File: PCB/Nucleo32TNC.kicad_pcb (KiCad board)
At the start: 2 copper layers, 66 x 99 mm, 54 parts, among them J1 AudioJack4, Q1 2N7000, Q2 2N7000, SW1 SW_Push, U1 MCP6004, U2 24LC32

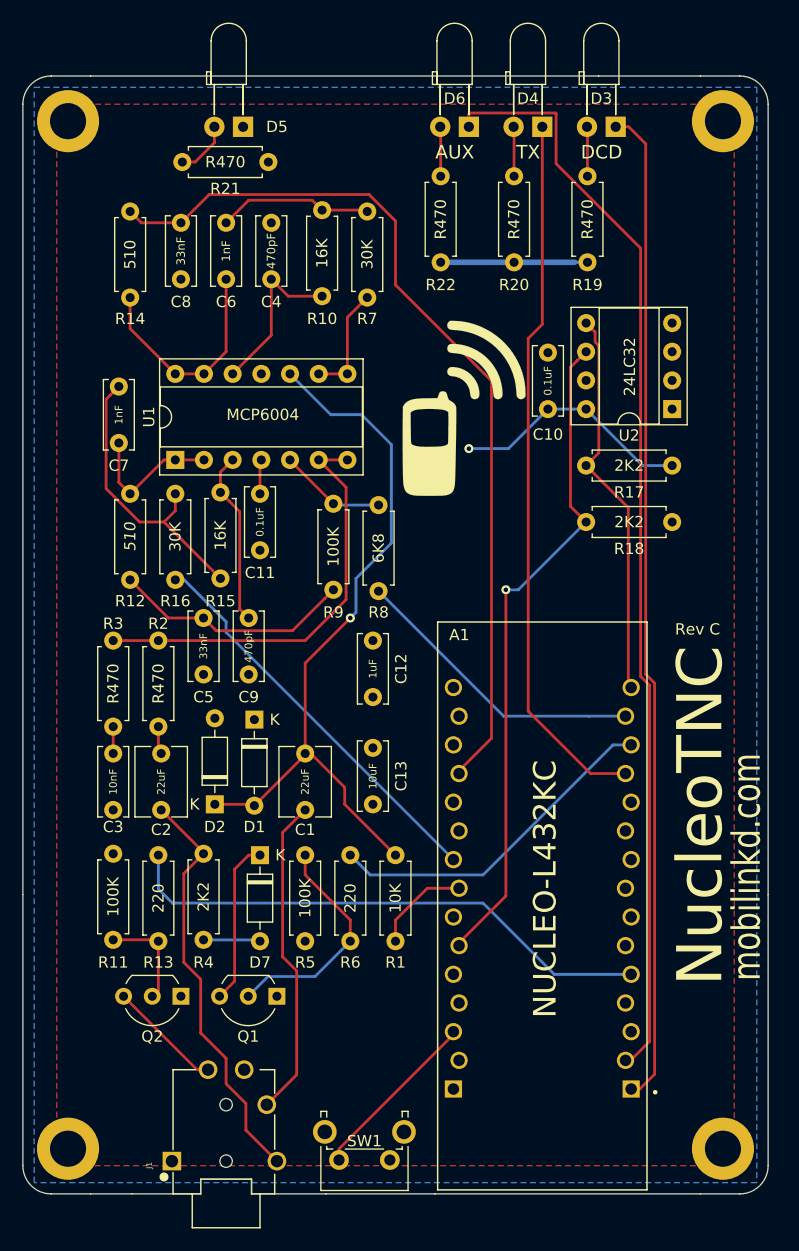
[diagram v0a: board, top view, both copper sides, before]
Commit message: Update files to KiCAD 7.
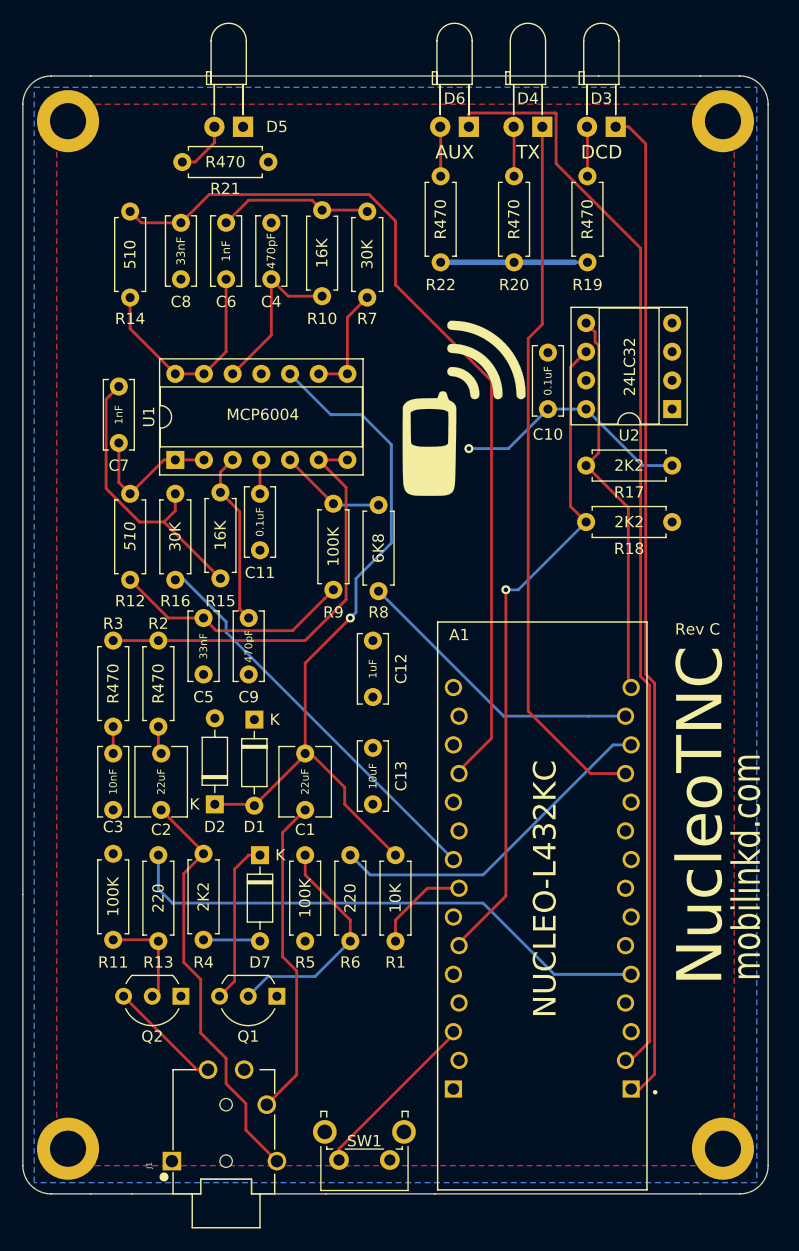
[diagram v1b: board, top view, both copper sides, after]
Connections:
- A1 pad 3.10: Net-(A1-Pad3.10) -> unconnected-(A1A-PF0-Pad3.10)
- A1 pad 3.11: Net-(A1-Pad3.11) -> unconnected-(A1A-PF1-Pad3.11)
- A1 pad 3.3: Net-(A1-Pad3.3) -> unconnected-(A1A-NRST-Pad3.3)
- A1 pad 3.6: Net-(A1-Pad3.6) -> unconnected-(A1A-PB0-Pad3.6)
- A1 pad 3.7: Net-(A1-Pad3.7) -> unconnected-(A1A-PB7-Pad3.7)
- A1 pad 3.8: Net-(A1-Pad3.8) -> unconnected-(A1A-PB6-Pad3.8)
- A1 pad 3.9: Net-(A1-Pad3.9) -> unconnected-(A1A-PB1-Pad3.9)
- A1 pad 4.1: Net-(A1-Pad4.1) -> unconnected-(A1B-VIN-Pad4.1)
- A1 pad 4.10: Net-(A1-Pad4.10) -> unconnected-(A1B-PA3-Pad4.10)
- A1 pad 4.11: Net-(A1-Pad4.11) -> unconnected-(A1B-PA1-Pad4.11)
- A1 pad 4.13: Net-(A1-Pad4.13) -> unconnected-(A1B-AREF-Pad4.13)
- A1 pad 4.15: Net-(A1-Pad4.15) -> unconnected-(A1B-PB3-Pad4.15)
- A1 pad 4.4: Net-(A1-Pad4.4) -> unconnected-(A1B-+5V-Pad4.4)
- A1 pad 4.5: Net-(A1-Pad4.5) -> unconnected-(A1B-PA2-Pad4.5)
- A1 pad 4.7: Net-(A1-Pad4.7) -> unconnected-(A1B-PA6-Pad4.7)
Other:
- net class Default removed
- net class Power removed
